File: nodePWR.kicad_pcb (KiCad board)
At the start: 2 copper layers, 58.9 x 20.5 mm, 15 parts, among them P1 Vin (4.5-30VDC), P2 USB (power only), P3 Node, P4 Serial I/O, SW1 Prgm, U1 bq25070

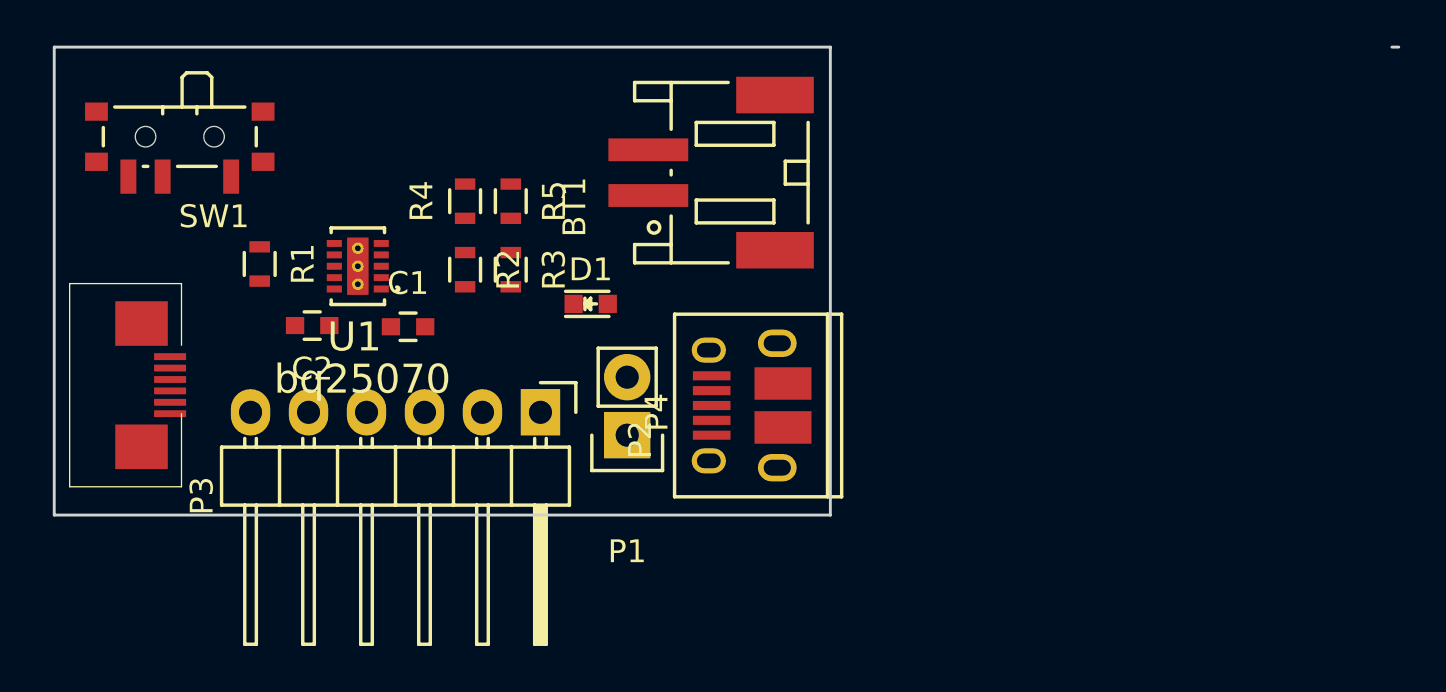
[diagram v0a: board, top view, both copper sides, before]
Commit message: Make board cut a polygon
On branch master
modified:   nodePWR.kicad_pcb
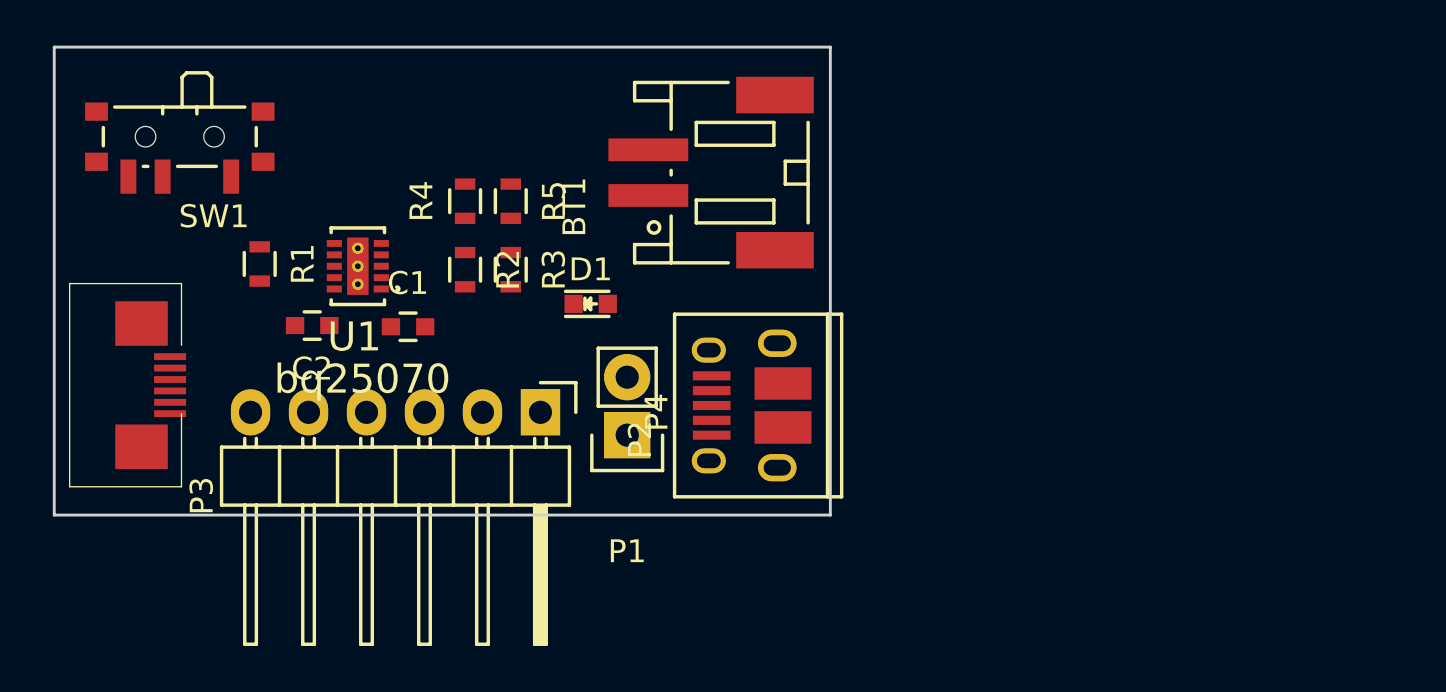
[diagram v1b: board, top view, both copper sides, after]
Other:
- board size 58.9 x 20.5 mm -> 34 x 20.5 mm
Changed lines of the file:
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@@
     (links 35)
     (no_connects 32)
-    (area 99.936499 99.0425 158.963501 126.875001)
+    (area 99.936499 99.0425 137.5675 126.875001)
     (thickness 1.6)
-    (drawings 5)
+    (drawings 4)
     (tracks 0)
     (zones 0)
@@
     )
   )
-  (gr_line (start 134 120.5) (end 134 100) (angle 90) (layer Edge.Cuts) (width 0.127))
-  (gr_line (start 158.6 100) (end 158.9 100) (angle 90) (layer Edge.Cuts) (width 0.127))
+  (gr_line (start 134 120.5) (end 100 120.5) (angle 90) (layer Edge.Cuts) (width 0.127))
+  (gr_line (start 134 100) (end 134 120.5) (angle 90) (layer Edge.Cuts) (width 0.127))
   (gr_line (start 100 100) (end 134 100) (angle 90) (layer Edge.Cuts) (width 0.127))
-  (gr_line (start 100 120.5) (end 134 120.5) (angle 90) (layer Edge.Cuts) (width 0.127))
-  (gr_line (start 100 100) (end 100 120.5) (angle 90) (layer Edge.Cuts) (width 0.127))
+  (gr_line (start 100 120.5) (end 100 100) (angle 90) (layer Edge.Cuts) (width 0.127))
 )

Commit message: Checkpoint: routed, no DRC errors
On branch master
modified:   nodePWR.kicad_pcb
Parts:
- moved R1 0.94 mm to (109.8, 109.1), turned to 180 degrees
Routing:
- net +BATT: track 0.00 -> 34.4 mm
- net GND: track 0.00 -> 22.6 mm, vias 0 -> 8
- net VDD: track 0.00 -> 17.8 mm
- net /TXD: track 0.00 -> 16.6 mm, vias 0 -> 1
- net Net-(D1-Pad1): track 0.00 -> 15.7 mm, vias 0 -> 2
- net /RXD: track 0.00 -> 13.4 mm, vias 0 -> 1
- net /PGM: track 0.00 -> 12.0 mm
- net /VCC: track 0.00 -> 10.0 mm, vias 0 -> 1
- net +3V3: track 0.00 -> 6.96 mm
- net Net-(R4-Pad2): track 0.00 -> 6.94 mm
- net Net-(D1-Pad2): track 0.00 -> 4.89 mm
- net Net-(R2-Pad1): track 0.00 -> 4.46 mm
- net Net-(R1-Pad1): track 0.00 -> 1.67 mm
- added copper zone on B.Cu, net GND
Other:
- net class Default: clearance 0.1524 -> 0.17; trace_width 0.1524 -> 0.17
- net class Power added: clearance 0.17, trace_width 0.3, via_dia 1, via_drill 0.4
- rule trace_clearance: 0.1524 -> 0.17

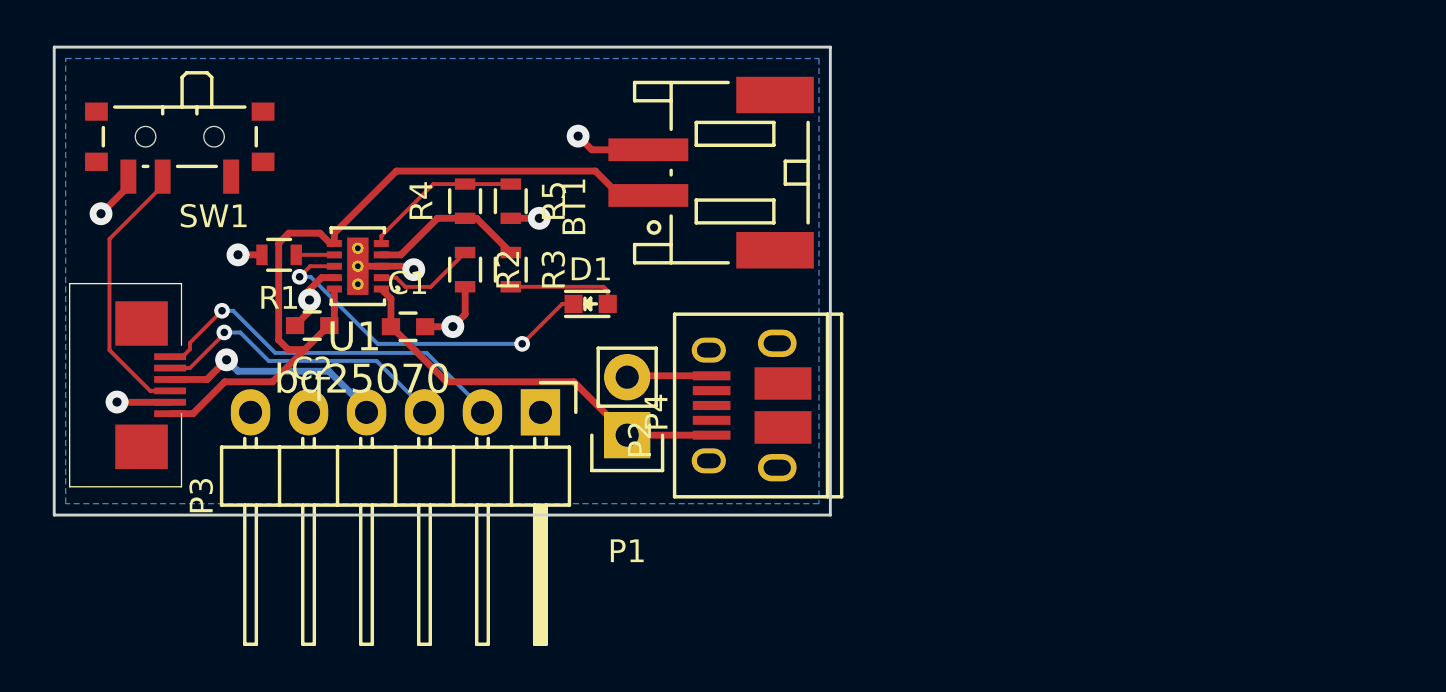
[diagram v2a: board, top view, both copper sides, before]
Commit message: Make changes to allow for an enclosure
    - move USB closer to PCB edge
    - Rotate BT1 so that connector can be used when there is an
      enclosure.
    - Add pins to solder in a battery.
    - change serial I/O header to veritical.
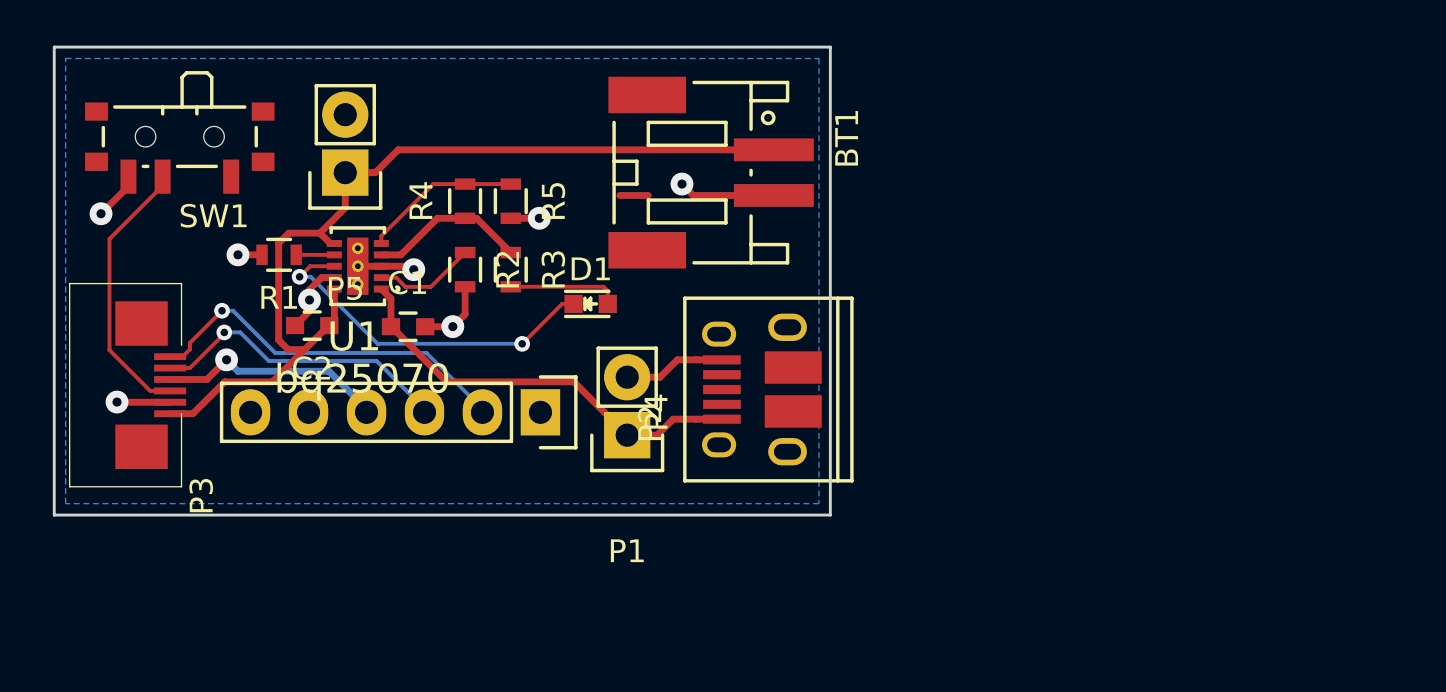
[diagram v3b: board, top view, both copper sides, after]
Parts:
- added P5: BAT, Pin_Headers:Pin_Header_Straight_1x02, F.Cu at (112.8, 105.5)
- P4: footprint Pin_Headers:Pin_Header_Angled_1x06 -> Pin_Headers:Pin_Header_Straight_1x06
- moved P2 0.83 mm to (130.8, 115.0)
- moved BT1 0.05 mm to (128.8, 105.5), turned to 270 degrees
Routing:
- net +BATT: track 34.4 -> 40.9 mm
- net GND: track 22.6 -> 24.4 mm
- net (no net): track 0.00 -> 1.25 mm
- net VDD: track 17.8 -> 18.6 mm

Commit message: Cleanup silk screen
On branch master
modified:   nodePWR.kicad_pcb
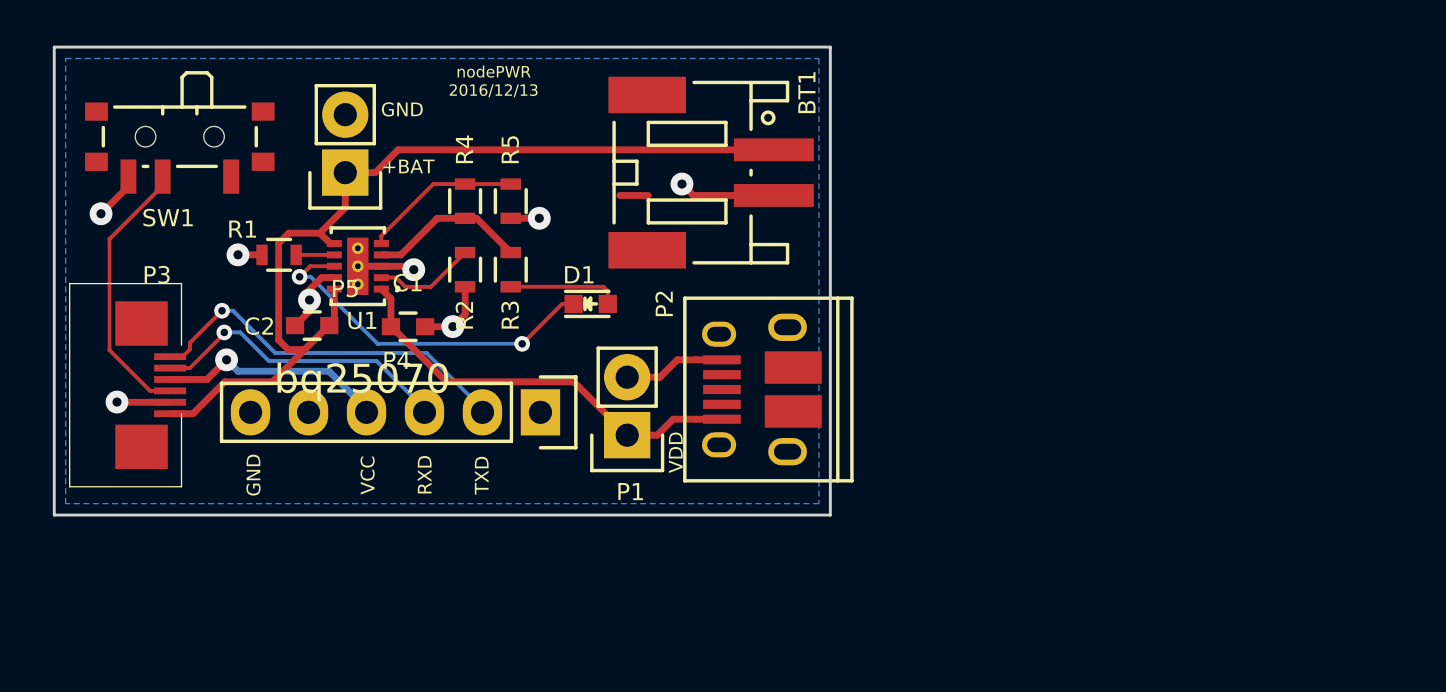
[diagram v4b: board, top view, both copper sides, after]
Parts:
- added Ref**: RockingDLogo_9x7, rockingDLogos:RockingDLogo_9x7, B.Cu at (107.5, 111.0)
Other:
- board text added: "+BAT"
- board text added: "Copyright 2016, J. Dunmire All Rights reserved. jerry@dunmire.org"
- board text added: "GND"
- board text added: "RXD"
- board text added: "TXD"
- board text added: "VCC"
- board text added: "VDD"
- board text added: "nodePWR 2016/12/13"

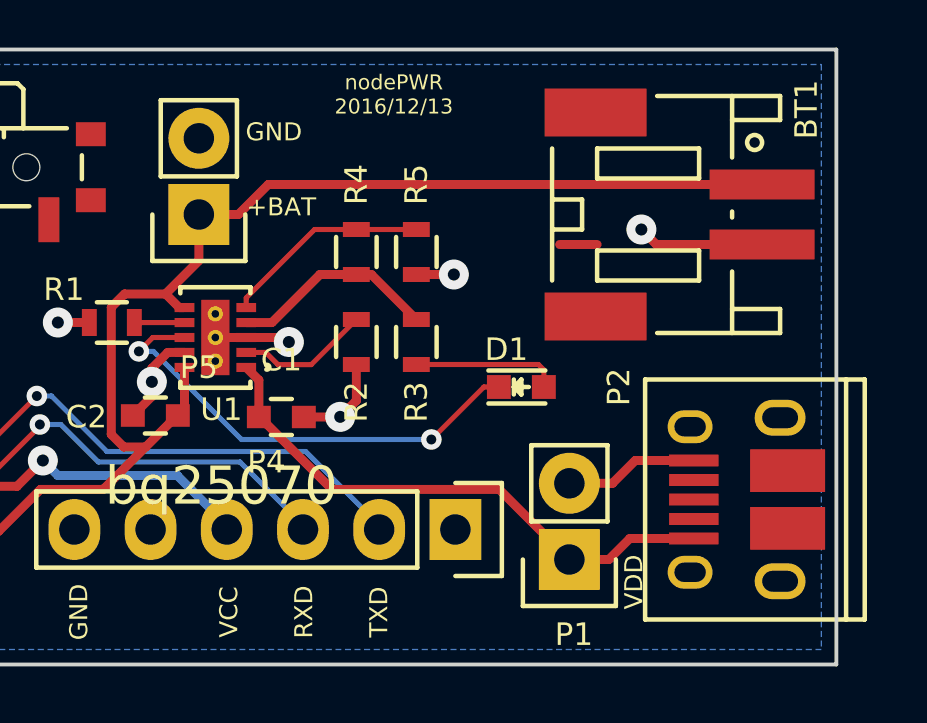
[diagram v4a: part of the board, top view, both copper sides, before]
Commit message: Clean-up tracks and vias
On branch master
modified:   nodePWR.kicad_pcb
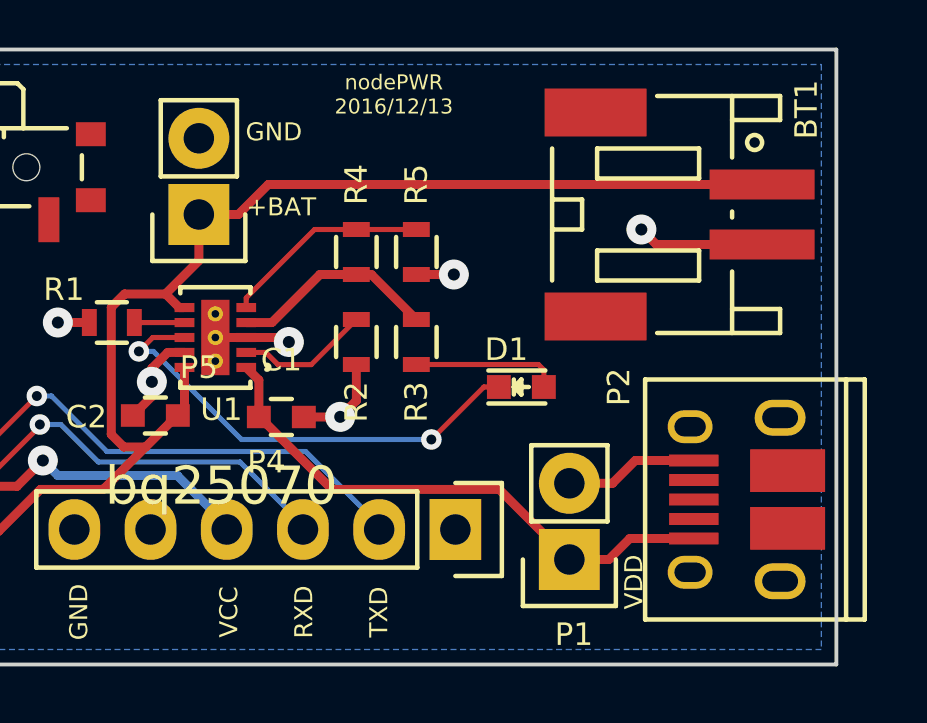
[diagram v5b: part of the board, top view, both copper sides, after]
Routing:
- net (no net): track 1.25 -> 0.00 mm

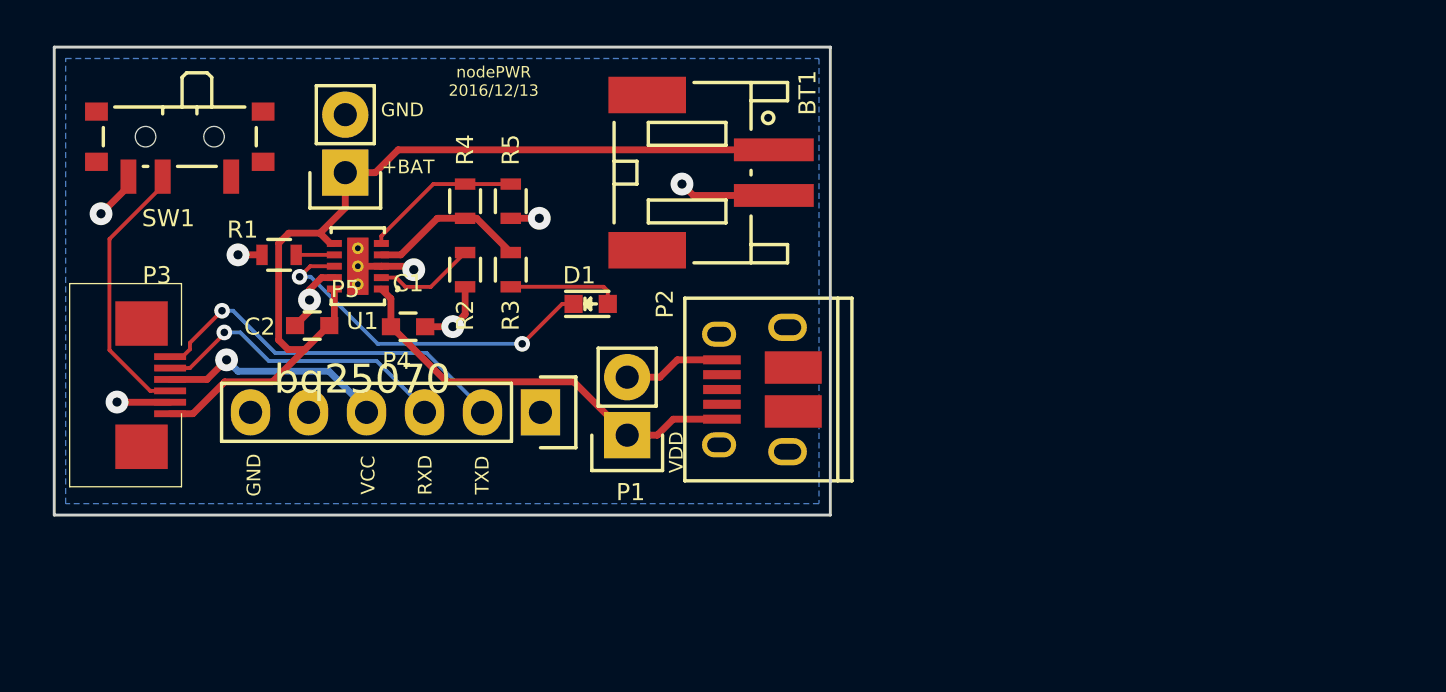
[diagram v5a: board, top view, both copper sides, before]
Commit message: Checkpoint - remove routing
    - preparing to add 7-pin connector and signals to the TLPHnode
      board.

On branch addChargerSignals
modified:   nodePWR.kicad_pcb
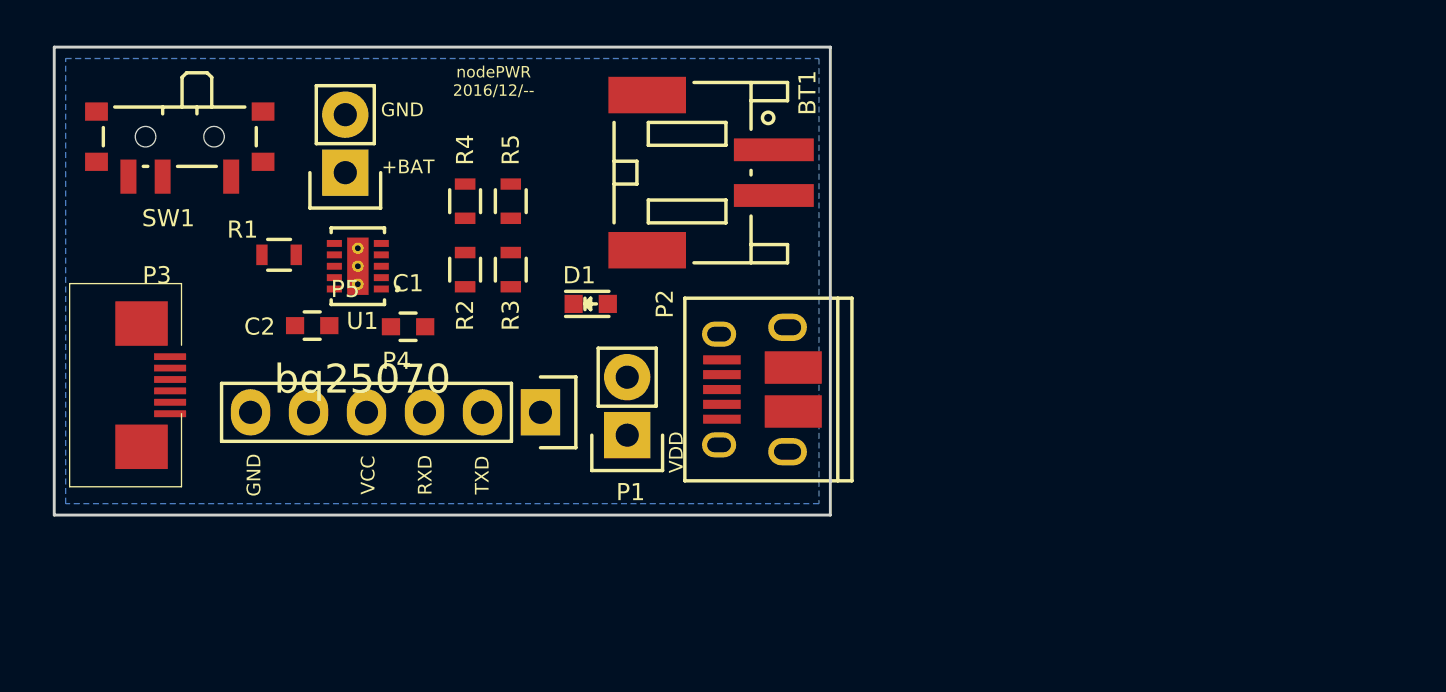
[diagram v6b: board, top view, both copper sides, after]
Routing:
- net +BATT: track 40.9 -> 0.00 mm
- net GND: track 24.4 -> 0.00 mm, vias 8 -> 0
- net VDD: track 18.6 -> 0.00 mm
- net /TXD: track 16.6 -> 0.00 mm, vias 1 -> 0
- net Net-(D1-Pad1): track 15.7 -> 0.00 mm, vias 2 -> 0
- net /RXD: track 13.4 -> 0.00 mm, vias 1 -> 0
- net /PGM: track 12.0 -> 0.00 mm
- net /VCC: track 10.0 -> 0.00 mm, vias 1 -> 0
- net +3V3: track 6.96 -> 0.00 mm
- net Net-(R4-Pad2): track 6.94 -> 0.00 mm
- net Net-(D1-Pad2): track 4.89 -> 0.00 mm
- net Net-(R2-Pad1): track 4.46 -> 0.00 mm
- net Net-(R1-Pad1): track 1.67 -> 0.00 mm
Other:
- board text added: "nodePWR 2016/12/--"
- board text removed: "nodePWR 2016/12/13"
